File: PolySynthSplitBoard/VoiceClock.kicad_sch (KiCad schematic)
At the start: 24 parts, among them U1001 74HC595, U1002 74HC595, U1003 4017, U1004 4017, U1005 4071

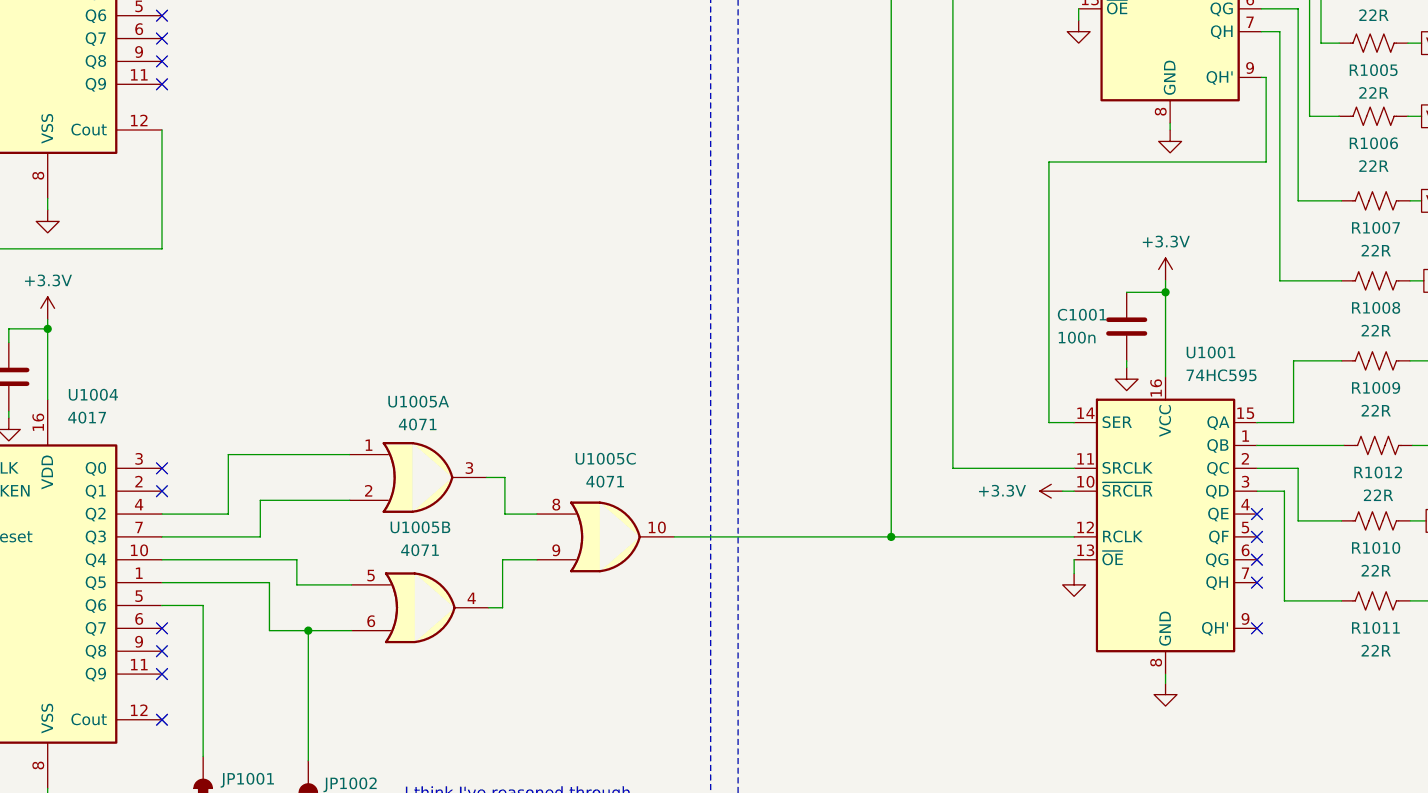
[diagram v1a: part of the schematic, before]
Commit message: double buffering voice clock fixes
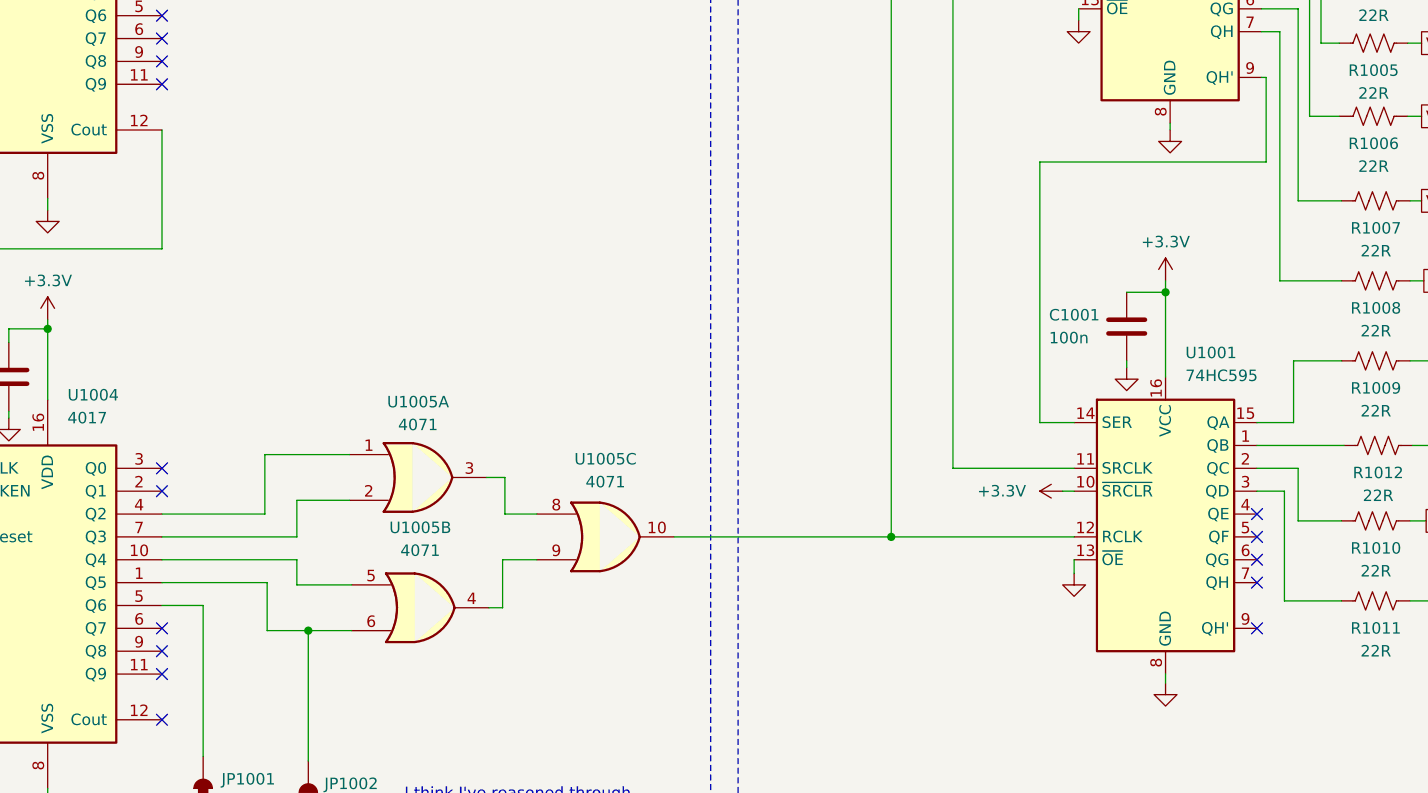
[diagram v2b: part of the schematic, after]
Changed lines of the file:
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@@
 	(wire
 		(pts
-			(xy 110.998 128.778) (xy 110.998 124.714)
+			(xy 115.062 128.778) (xy 115.062 124.714)
 		)
 		(stroke
@@
 	(wire
 		(pts
-			(xy 198.628 87.122) (xy 198.628 116.078)
+			(xy 197.612 87.122) (xy 197.612 116.078)
 		)
 		(stroke
@@
 	(wire
 		(pts
-			(xy 100.076 126.238) (xy 107.442 126.238)
+			(xy 100.076 126.238) (xy 111.506 126.238)
 		)
 		(stroke
@@
 	(wire
 		(pts
-			(xy 110.998 124.714) (xy 120.904 124.714)
+			(xy 115.062 124.714) (xy 120.904 124.714)
 		)
 		(stroke
@@
 	(wire
 		(pts
-			(xy 100.076 128.778) (xy 110.998 128.778)
+			(xy 100.076 128.778) (xy 115.062 128.778)
 		)
 		(stroke
@@
 	(wire
 		(pts
-			(xy 107.442 126.238) (xy 107.442 119.634)
+			(xy 111.506 126.238) (xy 111.506 119.634)
 		)
 		(stroke
@@
 	(wire
 		(pts
-			(xy 198.628 116.078) (xy 201.422 116.078)
+			(xy 197.612 116.078) (xy 201.422 116.078)
 		)
 		(stroke
@@
 	(wire
 		(pts
-			(xy 100.076 133.858) (xy 112.014 133.858)
+			(xy 100.076 133.858) (xy 111.76 133.858)
 		)
 		(stroke
@@
 	(wire
 		(pts
-			(xy 112.014 133.858) (xy 112.014 139.192)
+			(xy 111.76 133.858) (xy 111.76 139.192)
 		)
 		(stroke
@@
 	(wire
 		(pts
-			(xy 198.628 87.122) (xy 222.758 87.122)
+			(xy 197.612 87.122) (xy 222.758 87.122)
 		)
 		(stroke
@@
 	(wire
 		(pts
-			(xy 107.442 119.634) (xy 120.904 119.634)
+			(xy 111.506 119.634) (xy 120.904 119.634)
 		)
 		(stroke
@@
 	(wire
 		(pts
-			(xy 112.014 139.192) (xy 116.332 139.192)
+			(xy 111.76 139.192) (xy 116.332 139.192)
 		)
 		(stroke
@@
 		(dnp no)
 		(property "Reference" "C1001"
-			(at 199.517 104.14 0)
+			(at 198.628 104.14 0)
 			(effects
 				(font
@@
 		)
 		(property "Value" "100n"
-			(at 199.517 106.68 0)
+			(at 198.628 106.68 0)
 			(effects
 				(font
